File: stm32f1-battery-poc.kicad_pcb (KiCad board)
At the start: 4 copper layers, 92.5 x 85 mm, 153 parts, among them J1 Conn_01x02, J10 Conn_02x03_Odd_Even, J11 Conn_02x03_Odd_Even, J12 Conn_02x03_Odd_Even, J2 Conn_02x02_Odd_Even, J3 Conn_02x03_Odd_Even, J4 Conn_02x07_Odd_Even, J5 Conn_02x02_Odd_Even, J6 Conn_02x02_Odd_Even, J7 Conn_02x03_Odd_Even, J8 Conn_01x02, J9 Conn_01x04_Pin, M1 Stepper_Motor_bipolar, M2 Motor_3_Phases, Q1 Q_NMOS, Q2 Q_NMOS, SW1 SW_Push, SW2 SW_Push, SW3 SW_Push, SW4 SW_SPST, U1 LM78M05, U10 DRV8311H, U2 HT753-1, U3 SN65HVD230, U4 QRE1113GR, U5 QRE1113GR, U6 QRE1113GR, U7 DRV8424RGER, U8 STM32F103C8Tx, U9 BQ77905, Y1 8M

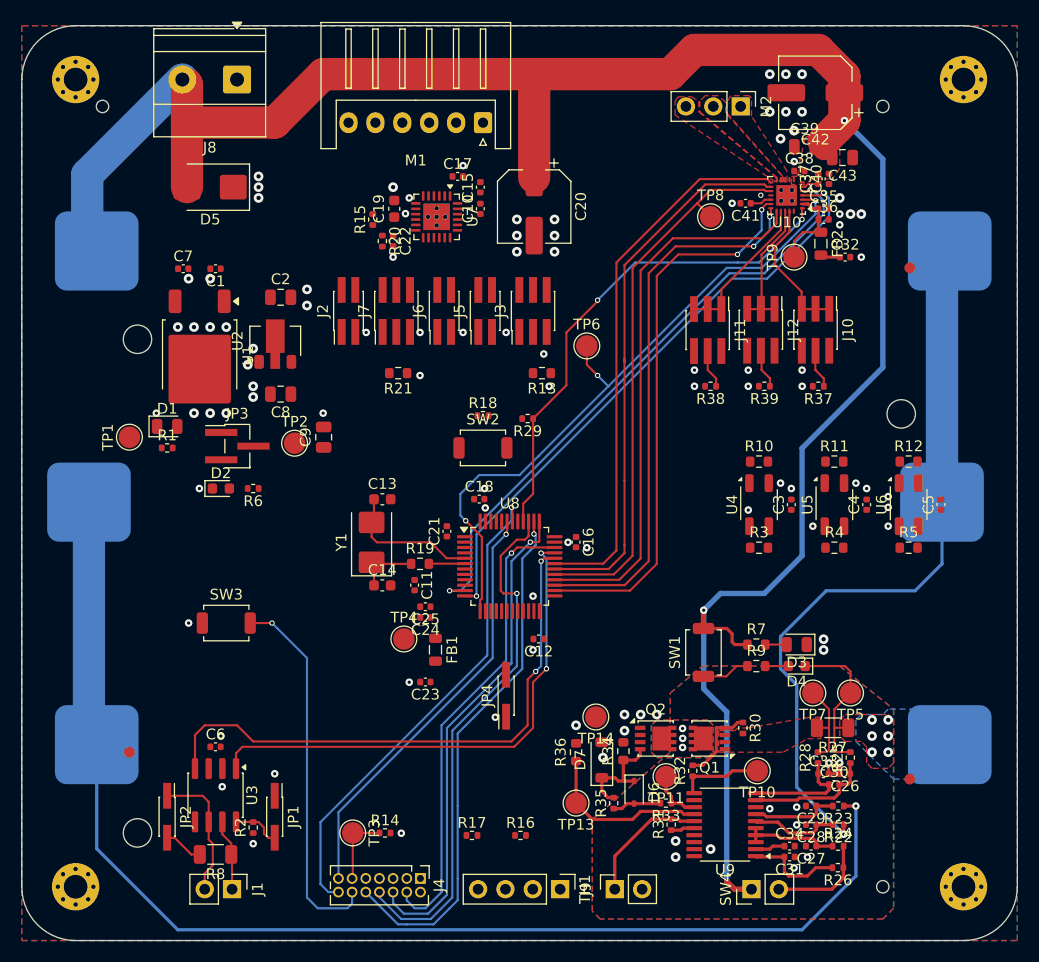
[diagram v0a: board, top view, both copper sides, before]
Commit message: pcb: add DRV8424 stepper driver routing
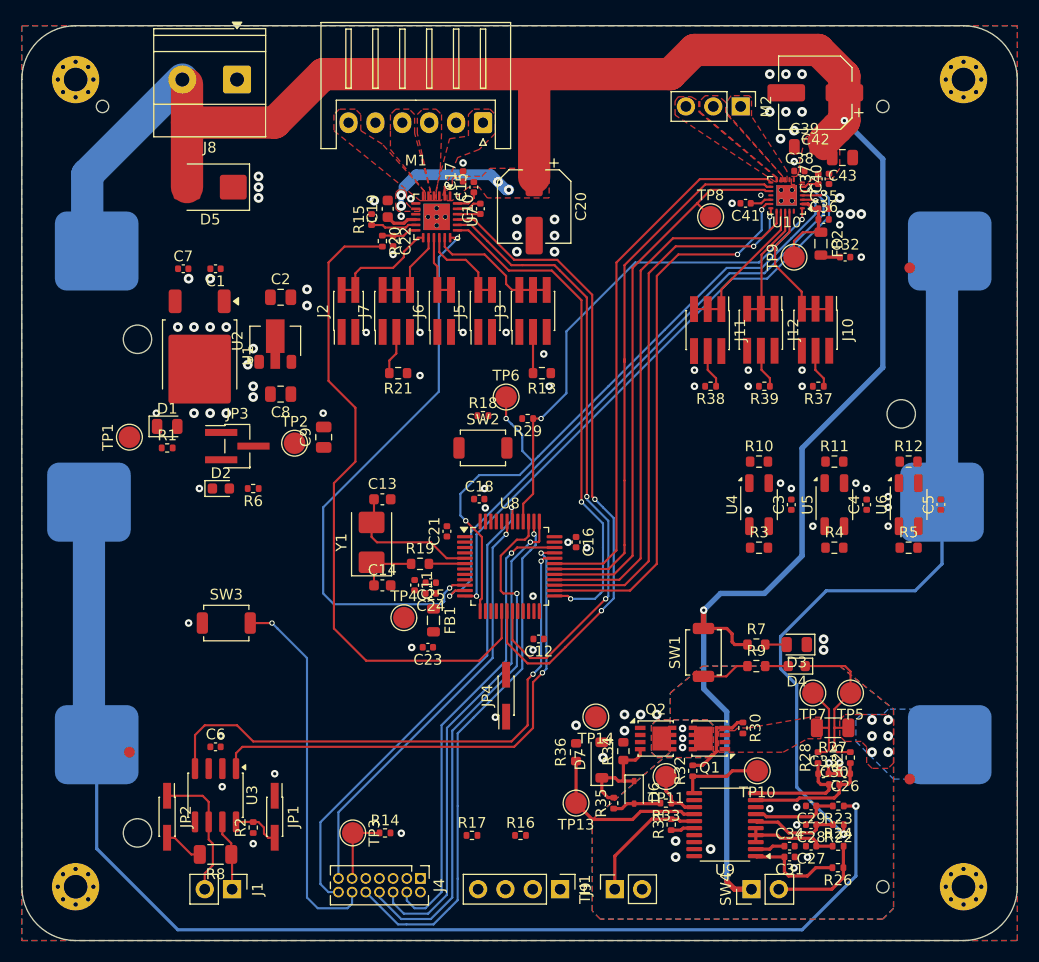
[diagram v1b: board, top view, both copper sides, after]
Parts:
- moved TP6 8.88 mm to (147.5, 77.0)
- moved C23 3.24 mm to (140.2, 100.2)
- moved FB1 2.74 mm to (140.8, 97.8)
- moved C24 2.29 mm to (140.5, 95.2)
- moved C25 2.29 mm to (140.5, 94.2)
- moved TP4 1.98 mm to (138.0, 97.5)
- moved C15 0.61 mm to (144.5, 57.5)
- moved C19 0.61 mm to (136.5, 59.5)
- moved C17 0.50 mm to (143.5, 56.5), turned to 90 degrees
- moved R15 0.11 mm to (135.0, 60.5)
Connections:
- U8 pad 18: /DIR -> /~{SLEEP}
- U8 pad 25: /~{SLEEP} -> /DIR
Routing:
- net /VPWM: track 0.00 -> 61.7 mm
- net /~{SLEEP}: track 0.00 -> 60.6 mm, vias 0 -> 2
- net /EN: track 0.00 -> 58.1 mm, vias 0 -> 2
- net /STEP: track 0.00 -> 53.7 mm, vias 0 -> 2
- net /DIR: track 0.00 -> 47.0 mm, vias 0 -> 2
- net +BATT: track 203.7 -> 216.4 mm, vias 2 -> 6
- net Net-(J3-Pin_2): track 0.00 -> 12.5 mm
- net Net-(J2-Pin_2): track 0.00 -> 10.8 mm
- net Net-(J5-Pin_2): track 0.00 -> 8.65 mm
- net Net-(J7-Pin_2): track 0.00 -> 8.11 mm
- net Net-(J6-Pin_2): track 0.00 -> 6.25 mm
- net Net-(U7-~{FAULT}): track 0.00 -> 4.30 mm
- net Net-(J7-Pin_3): track 0.00 -> 4.10 mm
- net Net-(J3-Pin_3): track 0.00 -> 3.83 mm
- net Net-(U7-VREF): track 0.00 -> 3.33 mm
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- added copper zone on F.Cu, net Net-(M1--)
- added copper zone on F.Cu, net Net-(U7-AOUT2)
- added copper zone on F.Cu, net Net-(U7-BOUT1)
- added copper zone on F.Cu, net Net-(U7-BOUT2)

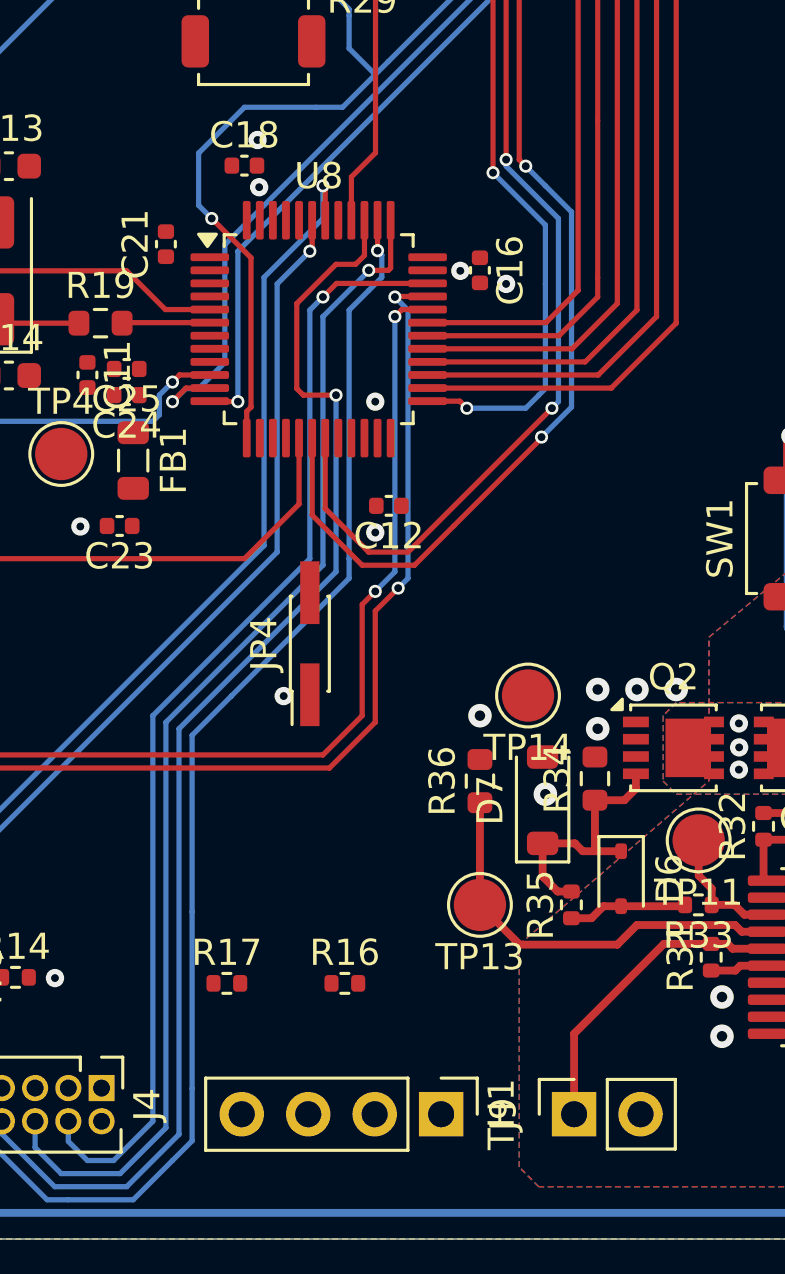
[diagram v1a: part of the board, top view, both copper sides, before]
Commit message: pcb: add I2C connector routing
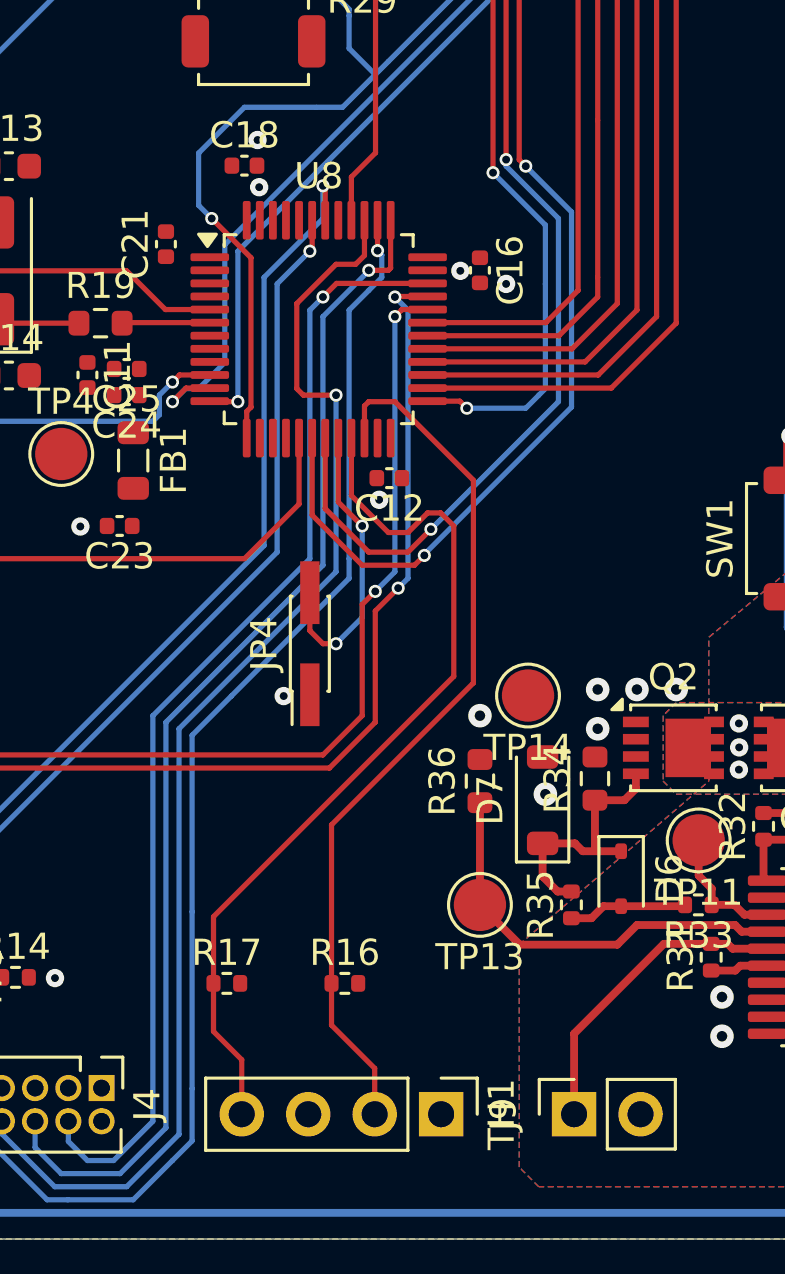
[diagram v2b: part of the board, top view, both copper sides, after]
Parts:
- moved C12 1.06 mm to (150.5, 98.4)
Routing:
- net /I2C2_SCL: track 0.00 -> 33.9 mm
- net /I2C2_SDA: track 0.00 -> 33.9 mm
- net Net-(JP4-B): track 0.00 -> 11.3 mm, vias 0 -> 2
- net GND: vias 94 -> 93

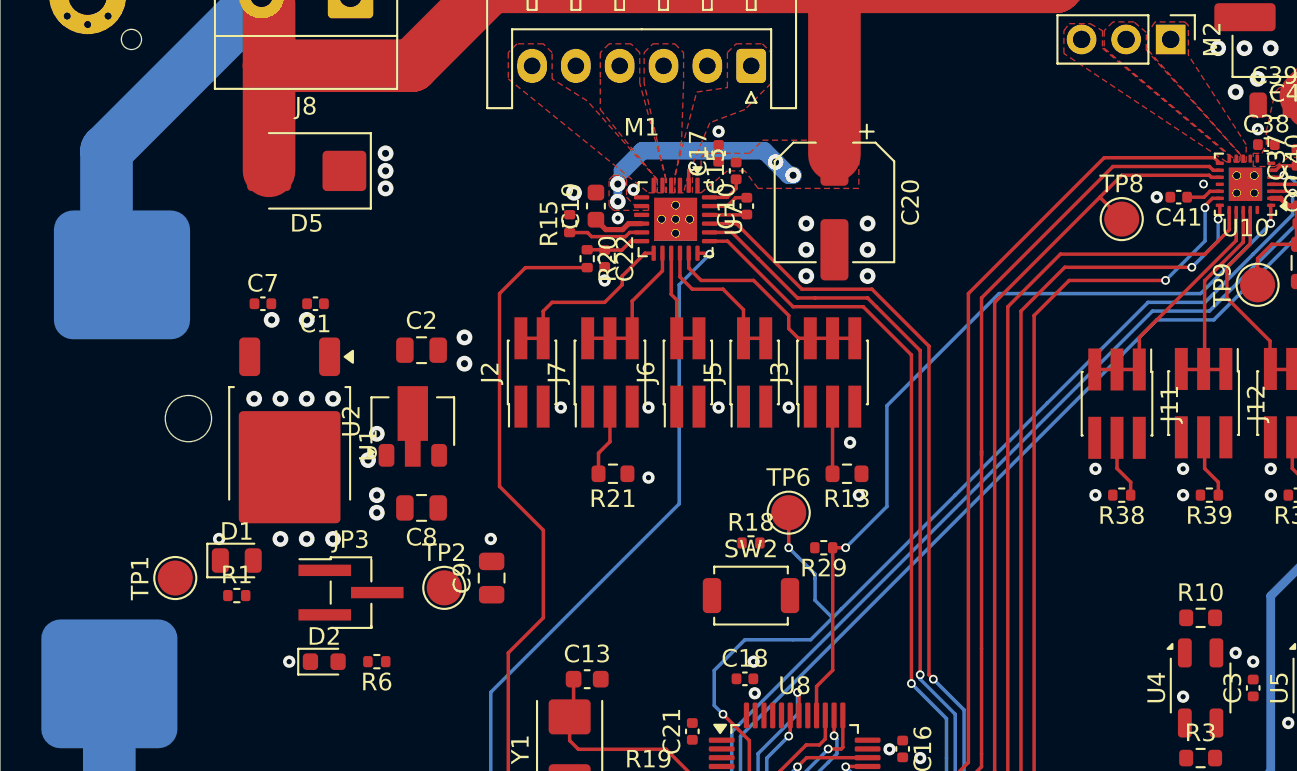
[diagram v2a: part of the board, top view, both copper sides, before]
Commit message: pcb: add power ldos routing
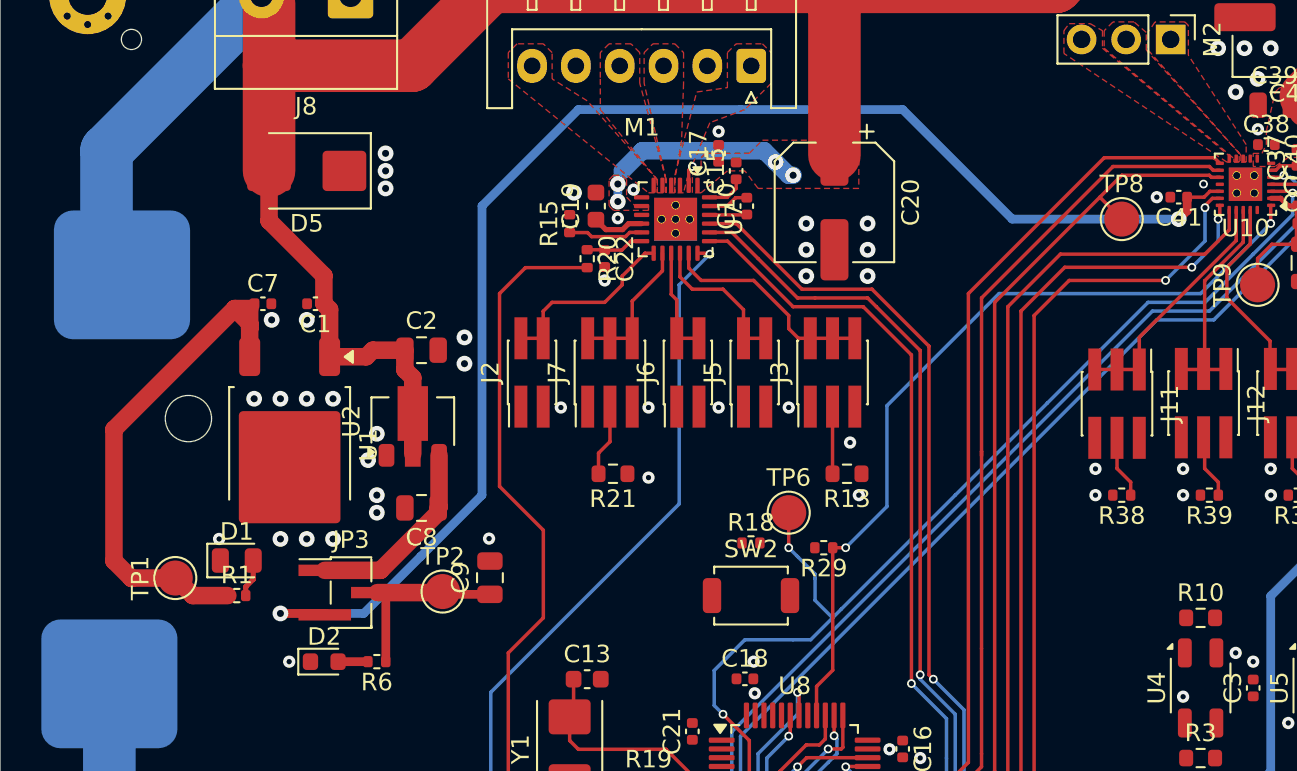
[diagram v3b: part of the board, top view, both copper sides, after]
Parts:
- moved TP2 0.23 mm to (127.8, 81.5)
- moved C9 0.10 mm to (130.5, 80.7)
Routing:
- net +DRV_3V3: track 2.00 -> 81.5 mm, vias 0 -> 2
- net +5V: track 0.00 -> 30.1 mm
- net +BATT: track 216.4 -> 239.0 mm
- net +3V3: track 1.55 -> 12.8 mm
- net Net-(JP3-A): track 0.00 -> 11.1 mm
- net Net-(D1-A): track 0.00 -> 2.18 mm
- net Net-(D2-A): track 0.00 -> 1.70 mm

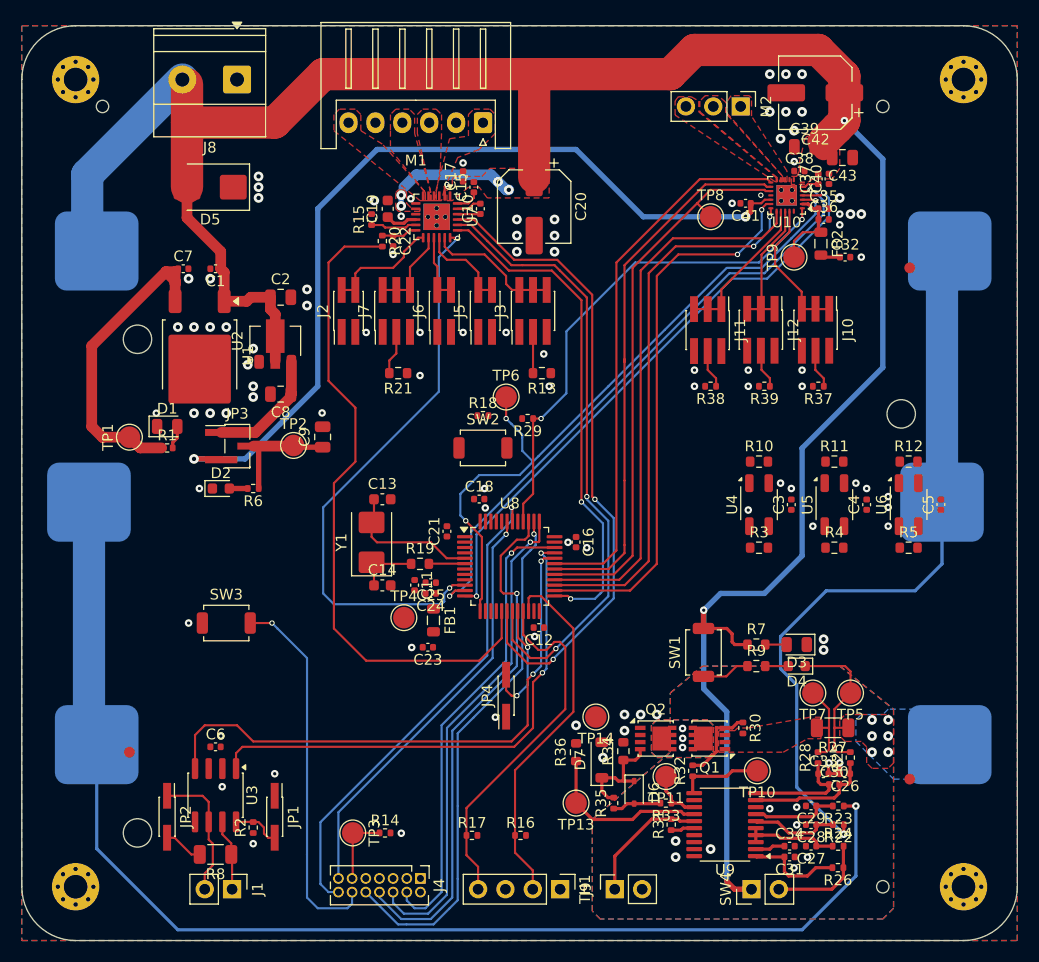
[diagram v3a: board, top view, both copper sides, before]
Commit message: pcb: add 3v3 power routing
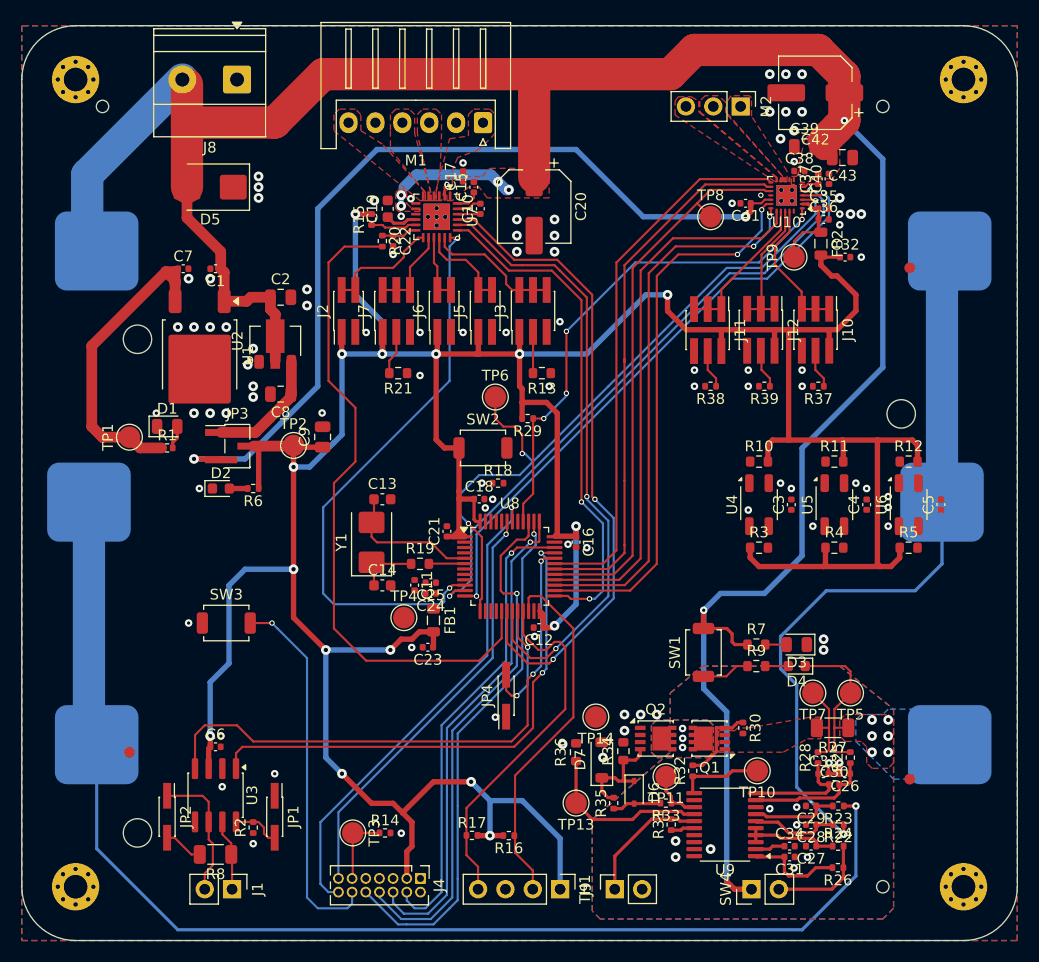
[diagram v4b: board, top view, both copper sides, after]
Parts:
- moved R18 6.42 mm to (146.8, 85.0)
- moved R16 1.09 mm to (147.8, 117.8), turned to 180 degrees
- moved TP6 1.00 mm to (146.5, 77.0)
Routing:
- net +3V3: track 12.8 -> 350.9 mm, vias 0 -> 16
- net /SOC: track 65.1 -> 66.2 mm
- net /~{FAULT}: track 47.0 -> 47.2 mm, vias 2 -> 4
- net GND: vias 93 -> 94
